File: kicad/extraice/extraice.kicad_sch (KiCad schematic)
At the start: 71 parts, among them J1 Conn_01x02, J10 Conn_01x02, J3 EncSide, J4 MainSide, J5 Conn_01x05, J6 EncSide, J7 MainSide, J8 Conn_01x02, J9 Conn_01x02, Q1 L-31ROPT1C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

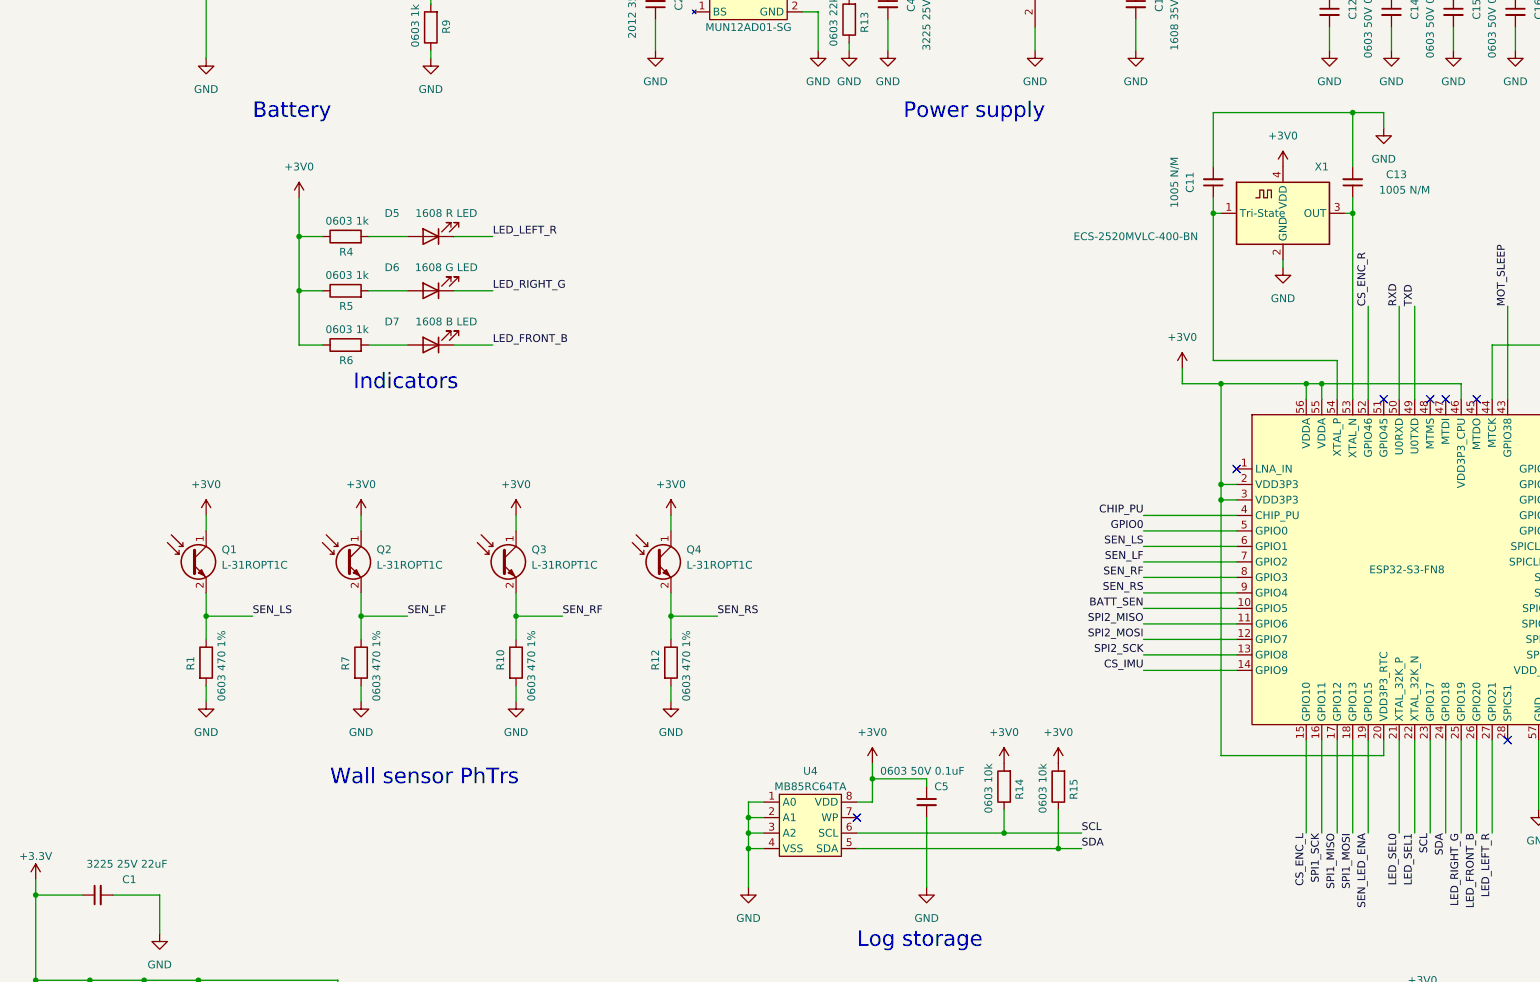
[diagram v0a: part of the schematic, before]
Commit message: Fix problems identified during implementation
- ESP32 supports only crystal oscillator, not resonator.
- The package and capacitance of capacitor C1 were incorrect.
- Fix a ESP32 pin name. GPIO15 -> GPIO14.

Signed-off-by: Kazuki Iida <elkel53930@gmail.com>
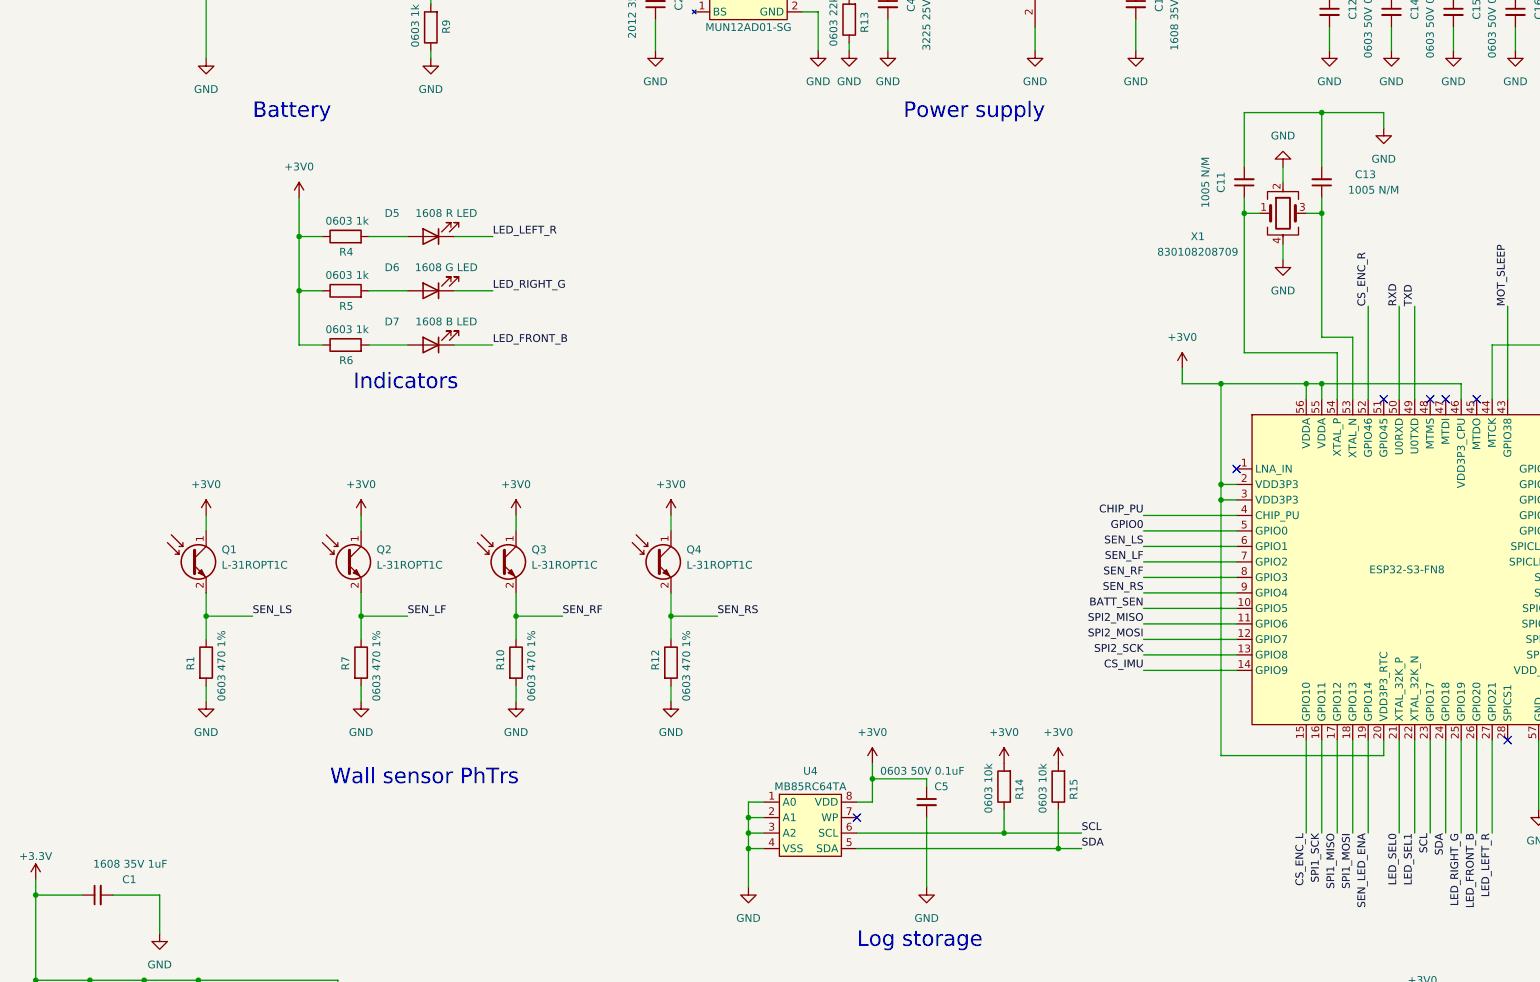
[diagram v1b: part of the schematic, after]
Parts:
- removed X1: ECS-2520MVLC-400-BN, Oscillator:Oscillator_SMD_ECS_2520MV-xxx-xx-4Pin_2.5x2.0mm, symbol Oscillator:ECS-2520MV-xxx-xx
- added X1: 830108208709, Oscillator:Oscillator_SMD_ECS_2520MV-xxx-xx-4Pin_2.5x2.0mm, symbol Device:Crystal_GND24
- C1: value 3225 25V 22uF -> 1608 35V 1uF
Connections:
- net GND: now also X1.2, X1.4
- net at C11.1, U7.54 (XTAL_P): now also X1.1
- net at C13.1, U7.53 (XTAL_N): now also X1.3
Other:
- moved on the sheet: C11, C13
